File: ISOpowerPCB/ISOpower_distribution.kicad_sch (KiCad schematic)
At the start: 28 parts

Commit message: significant changes
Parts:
- added JP?: DSBL_BYPSS_A, symbol Jumper:SolderJumper_2_Open
- added JP?: DSBL_BYPSS_B, symbol Jumper:SolderJumper_2_Open
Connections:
- net GND: now also JP?.1 (A), JP?.1 (A)
- net at Q?.3 (S), U?.2 (On/Off): now also JP?.2 (B) (x2)
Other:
- moved on the sheet: C?
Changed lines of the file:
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@@
   (junction (at 41.91 143.51) (diameter 0) (color 0 0 0 0)
   )
+  (junction (at 50.8 166.37) (diameter 0) (color 0 0 0 0)
+  )
   (junction (at 57.15 87.63) (diameter 0) (color 0 0 0 0)
   )
@@
   (junction (at 207.01 74.93) (diameter 0) (color 0 0 0 0)
   )
+  (junction (at 59.69 153.67) (diameter 0) (color 0 0 0 0)
+  )
   (junction (at 107.95 64.77) (diameter 0) (color 0 0 0 0)
   )
@@
   (junction (at 158.75 130.81) (diameter 0) (color 0 0 0 0)
   )
-  (junction (at 40.64 64.77) (diameter 0) (color 0 0 0 0)
+  (junction (at 35.56 64.77) (diameter 0) (color 0 0 0 0)
   )
   (junction (at 90.17 87.63) (diameter 0) (color 0 0 0 0)
@@
   (junction (at 90.17 64.77) (diameter 0) (color 0 0 0 0)
   )
+  (junction (at 48.26 87.63) (diameter 0) (color 0 0 0 0)
+  )
   (junction (at 250.19 44.45) (diameter 0) (color 0 0 0 0)
   )
@@
   (junction (at 157.48 52.07) (diameter 0) (color 0 0 0 0)
   )
-  (junction (at 40.64 87.63) (diameter 0) (color 0 0 0 0)
+  (junction (at 35.56 87.63) (diameter 0) (color 0 0 0 0)
   )
   (junction (at 214.63 143.51) (diameter 0) (color 0 0 0 0)
+  )
+  (junction (at 57.15 74.93) (diameter 0) (color 0 0 0 0)
   )
   (junction (at 107.95 87.63) (diameter 0) (color 0 0 0 0)
@@
     (stroke (width 0) (type default) (color 0 0 0 0))
   )
-  (wire (pts (xy 39.37 80.01) (xy 41.91 80.01))
+  (wire (pts (xy 34.29 80.01) (xy 36.83 80.01))
     (stroke (width 0) (type default) (color 0 0 0 0))
   )
@@
     (stroke (width 0) (type default) (color 0 0 0 0))
   )
-  (wire (pts (xy 31.75 81.28) (xy 39.37 81.28))
+  (wire (pts (xy 26.67 81.28) (xy 34.29 81.28))
     (stroke (width 0) (type default) (color 0 0 0 0))
   )
@@
     (stroke (width 0) (type default) (color 0 0 0 0))
   )
+  (wire (pts (xy 50.8 166.37) (xy 59.69 166.37))
+    (stroke (width 0) (type default) (color 0 0 0 0))
+  )
   (wire (pts (xy 269.24 57.15) (xy 269.24 44.45))
     (stroke (width 0) (type default) (color 0 0 0 0))
@@
     (stroke (width 0) (type default) (color 0 0 0 0))
   )
+  (wire (pts (xy 57.15 74.93) (xy 48.26 74.93))
+    (stroke (width 0) (type default) (color 0 0 0 0))
+  )
   (wire (pts (xy 107.95 87.63) (xy 107.95 80.01))
     (stroke (width 0) (type default) (color 0 0 0 0))
@@
     (stroke (width 0) (type default) (color 0 0 0 0))
   )
+  (wire (pts (xy 50.8 163.83) (xy 50.8 166.37))
+    (stroke (width 0) (type default) (color 0 0 0 0))
+  )
   (wire (pts (xy 87.63 156.21) (xy 91.44 156.21))
     (stroke (width 0) (type default) (color 0 0 0 0))
@@
     (stroke (width 0) (type default) (color 0 0 0 0))
   )
-  (wire (pts (xy 39.37 81.28) (xy 39.37 80.01))
+  (wire (pts (xy 34.29 81.28) (xy 34.29 80.01))
     (stroke (width 0) (type default) (color 0 0 0 0))
   )
@@
     (stroke (width 0) (type default) (color 0 0 0 0))
   )
+  (wire (pts (xy 48.26 74.93) (xy 48.26 77.47))
+    (stroke (width 0) (type default) (color 0 0 0 0))
+  )
   (wire (pts (xy 59.69 166.37) (xy 63.5 166.37))
     (stroke (width 0) (type default) (color 0 0 0 0))
   )
-  (wire (pts (xy 40.64 77.47) (xy 40.64 87.63))
-    (stroke (width 0) (type default) (color 0 0 0 0))
-  )
-  (wire (pts (xy 41.91 166.37) (xy 59.69 166.37))
+  (wire (pts (xy 35.56 77.47) (xy 35.56 87.63))
+    (stroke (width 0) (type default) (color 0 0 0 0))
+  )
+  (wire (pts (xy 41.91 166.37) (xy 50.8 166.37))
     (stroke (width 0) (type default) (color 0 0 0 0))
   )
@@
     (stroke (width 0) (type default) (color 0 0 0 0))
   )
-  (wire (pts (xy 41.91 80.01) (xy 41.91 81.28))
+  (wire (pts (xy 36.83 80.01) (xy 36.83 81.28))
     (stroke (width 0) (type default) (color 0 0 0 0))
   )
@@
     (stroke (width 0) (type default) (color 0 0 0 0))
   )
-  (wire (pts (xy 40.64 64.77) (xy 62.23 64.77))
-    (stroke (width 0) (type default) (color 0 0 0 0))
-  )
   (wire (pts (xy 109.22 173.99) (xy 109.22 166.37))
     (stroke (width 0) (type default) (color 0 0 0 0))
@@
     (stroke (width 0) (type default) (color 0 0 0 0))
   )
+  (wire (pts (xy 35.56 64.77) (xy 62.23 64.77))
+    (stroke (width 0) (type default) (color 0 0 0 0))
+  )
   (wire (pts (xy 203.2 128.27) (xy 205.74 128.27))
     (stroke (width 0) (type default) (color 0 0 0 0))
@@
     (stroke (width 0) (type default) (color 0 0 0 0))
   )
-  (wire (pts (xy 40.64 87.63) (xy 57.15 87.63))
+  (wire (pts (xy 35.56 87.63) (xy 48.26 87.63))
     (stroke (width 0) (type default) (color 0 0 0 0))
   )
@@
     (stroke (width 0) (type default) (color 0 0 0 0))
   )
-  (wire (pts (xy 40.64 87.63) (xy 40.64 95.25))
+  (wire (pts (xy 35.56 87.63) (xy 35.56 95.25))
     (stroke (width 0) (type default) (color 0 0 0 0))
   )
@@
     (stroke (width 0) (type default) (color 0 0 0 0))
   )
+  (wire (pts (xy 48.26 85.09) (xy 48.26 87.63))
+    (stroke (width 0) (type default) (color 0 0 0 0))
+  )
   (wire (pts (xy 154.94 130.81) (xy 158.75 130.81))
     (stroke (width 0) (type default) (color 0 0 0 0))
@@
     (stroke (width 0) (type default) (color 0 0 0 0))
   )
+  (wire (pts (xy 48.26 87.63) (xy 57.15 87.63))
+    (stroke (width 0) (type default) (color 0 0 0 0))
+  )
   (wire (pts (xy 158.75 125.73) (xy 158.75 130.81))
     (stroke (width 0) (type default) (color 0 0 0 0))
@@
     (stroke (width 0) (type default) (color 0 0 0 0))
   )
-  (wire (pts (xy 35.56 64.77) (xy 40.64 64.77))
-    (stroke (width 0) (type default) (color 0 0 0 0))
-  )
   (wire (pts (xy 139.7 143.51) (xy 139.7 140.97))
     (stroke (width 0) (type default) (color 0 0 0 0))
@@
     (stroke (width 0) (type default) (color 0 0 0 0))
   )
-  (wire (pts (xy 40.64 64.77) (xy 40.64 69.85))
+  (wire (pts (xy 35.56 64.77) (xy 35.56 69.85))
     (stroke (width 0) (type default) (color 0 0 0 0))
   )
@@
     (stroke (width 0) (type default) (color 0 0 0 0))
   )
-  (wire (pts (xy 41.91 81.28) (xy 49.53 81.28))
+  (wire (pts (xy 50.8 153.67) (xy 59.69 153.67))
+    (stroke (width 0) (type default) (color 0 0 0 0))
+  )
+  (wire (pts (xy 36.83 81.28) (xy 49.53 81.28))
+    (stroke (width 0) (type default) (color 0 0 0 0))
+  )
+  (wire (pts (xy 50.8 156.21) (xy 50.8 153.67))
     (stroke (width 0) (type default) (color 0 0 0 0))
   )
@@
     (effects (font (size 1.27 1.27)) (justify right))
   )
-  (hierarchical_label "BUS_A_DISABLE" (shape input) (at 31.75 81.28 180)
+  (hierarchical_label "BUS_A_DISABLE" (shape input) (at 26.67 81.28 180)
     (effects (font (size 1.27 1.27)) (justify right))
   )
@@
     (pin "2")
   )
-  (symbol (lib_id "Device:100u") (at 40.64 73.66 0) (unit 1)
-    (in_bom yes) (on_board yes) (fields_autoplaced)
-    (property "Reference" "C?" (id 0) (at 44.45 71.5009 0)
-      (effects (font (size 1.27 1.27)) (justify left))
-    )
-    (property "Value" "100u" (id 1) (at 44.45 74.0409 0)
-      (effects (font (size 1.27 1.27)) (justify left))
-    )
-    (property "Footprint" "Capacitor_SMD:CP_Elec_10x10" (id 2) (at 41.6052 77.47 0)
-      (effects (font (size 1.27 1.27)) hide)
-    )
-    (property "Datasheet" "~" (id 3) (at 40.64 73.66 0)
+  (symbol (lib_id "Device:100u") (at 35.56 73.66 0) (unit 1)
+    (in_bom yes) (on_board yes) (fields_autoplaced)
+    (property "Reference" "C?" (id 0) (at 39.37 71.5009 0)
+      (effects (font (size 1.27 1.27)) (justify left))
+    )
+    (property "Value" "100u" (id 1) (at 39.37 74.0409 0)
+      (effects (font (size 1.27 1.27)) (justify left))
+    )
+    (property "Footprint" "Capacitor_SMD:CP_Elec_10x10" (id 2) (at 36.5252 77.47 0)
+      (effects (font (size 1.27 1.27)) hide)
+    )
+    (property "Datasheet" "~" (id 3) (at 35.56 73.66 0)
       (effects (font (size 1.27 1.27)) hide)
     )
@@
     (pin "14")
     (pin "7")
+  )
+  (symbol (lib_id "Jumper:SolderJumper_2_Open") (at 48.26 81.28 90) (unit 1)
+    (in_bom yes) (on_board yes)
+    (property "Reference" "JP?" (id 0) (at 45.72 86.36 90))
+    (property "Value" "DSBL_BYPSS_A" (id 1) (at 46.99 90.17 90))
+    (property "Footprint" "" (id 2) (at 48.26 81.28 0)
+      (effects (font (size 1.27 1.27)) hide)
+    )
+    (property "Datasheet" "~" (id 3) (at 48.26 81.28 0)
+      (effects (font (size 1.27 1.27)) hide)
+    )
+    (pin "1")
+    (pin "2")
   )
   (symbol (lib_id "power:GND") (at 109.22 173.99 0) (unit 1)
@@
     (pin "1")
   )
-  (symbol (lib_id "power:GND") (at 40.64 95.25 0) (unit 1)
-    (in_bom yes) (on_board yes) (fields_autoplaced)
-    (property "Reference" "#PWR?" (id 0) (at 40.64 101.6 0)
-      (effects (font (size 1.27 1.27)) hide)
-    )
-    (property "Value" "GND" (id 1) (at 40.64 100.33 0))
-    (property "Footprint" "" (id 2) (at 40.64 95.25 0)
-      (effects (font (size 1.27 1.27)) hide)
-    )
-    (property "Datasheet" "" (id 3) (at 40.64 95.25 0)
-      (effects (font (size 1.27 1.27)) hide)
-    )
+  (symbol (lib_id "Jumper:SolderJumper_2_Open") (at 50.8 160.02 90) (unit 1)
+    (in_bom yes) (on_board yes)
+    (property "Reference" "JP?" (id 0) (at 48.26 165.1 90))
+    (property "Value" "DSBL_BYPSS_B" (id 1) (at 49.53 168.91 90))
+    (property "Footprint" "" (id 2) (at 50.8 160.02 0)
+      (effects (font (size 1.27 1.27)) hide)
+    )
+    (property "Datasheet" "~" (id 3) (at 50.8 160.02 0)
+      (effects (font (size 1.27 1.27)) hide)
+    )
+    (pin "1")
+    (pin "2")
+  )
+  (symbol (lib_id "power:GND") (at 35.56 95.25 0) (unit 1)
+    (in_bom yes) (on_board yes) (fields_autoplaced)
+    (property "Reference" "#PWR?" (id 0) (at 35.56 101.6 0)
+      (effects (font (size 1.27 1.27)) hide)
+    )
+    (property "Value" "GND" (id 1) (at 35.56 100.33 0))
+    (property "Footprint" "" (id 2) (at 35.56 95.25 0)
+      (effects (font (size 1.27 1.27)) hide)
+    )
+    (property "Datasheet" "" (id 3) (at 35.56 95.25 0)
+      (effects (font (size 1.27 1.27)) hide)
+    )

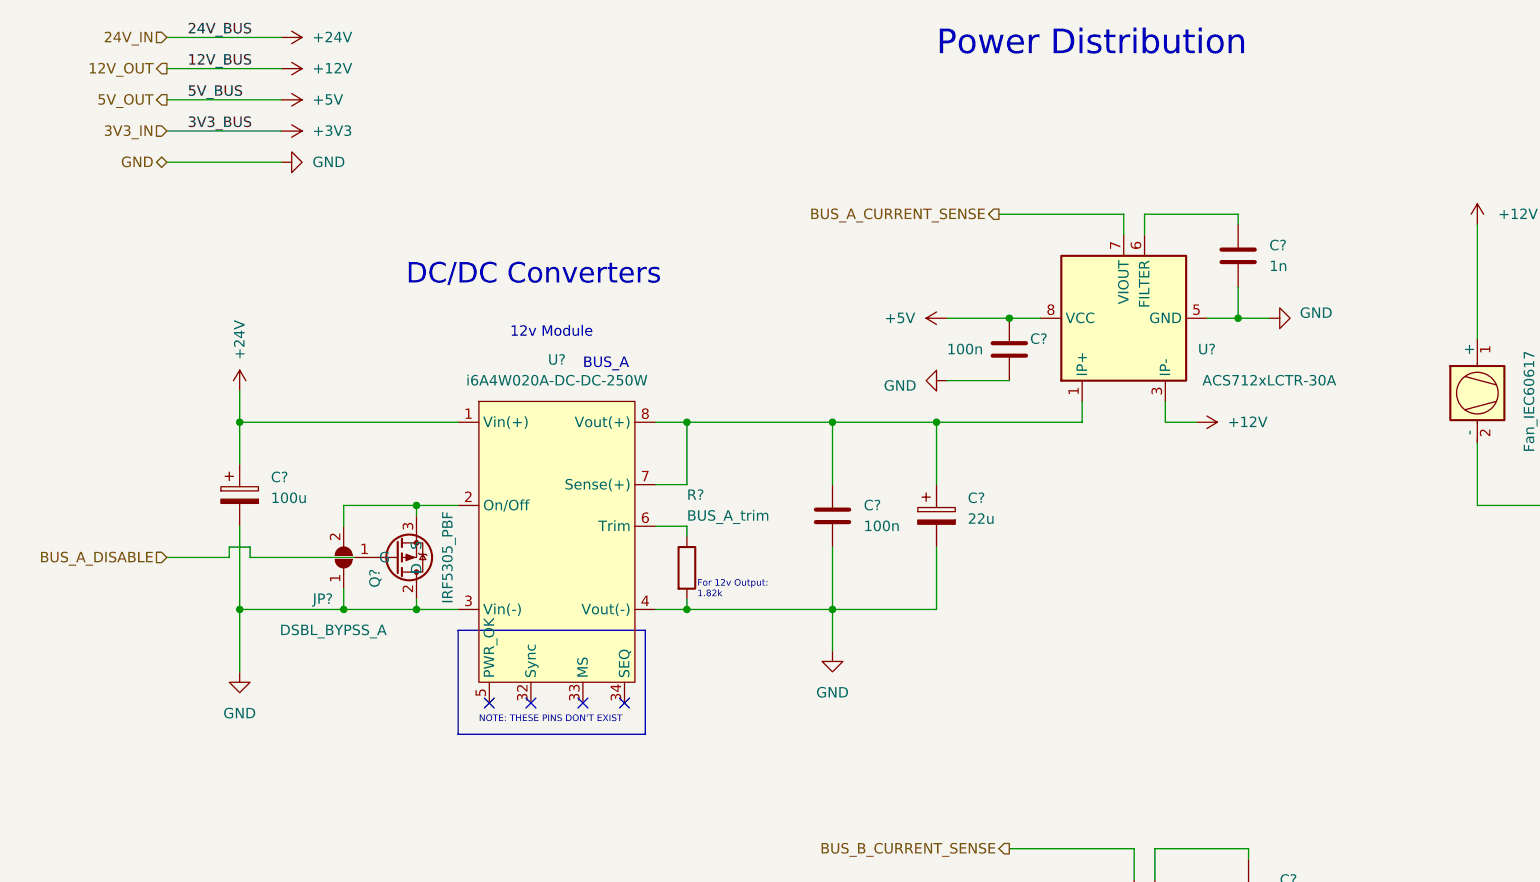
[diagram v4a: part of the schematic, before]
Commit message: Updated as per discussions 26/01/22
# Change Notes

04/02/2022
As per discussion 26/01/22
1. Changed per channel 5v MOSFET switches to MOSFET control of DC/DC module on/off pin - due to failure of MOSFET switching during testing.
2. Added 5v buck converter for independent MCU_5V power bus.
	- Ensured all 5v MCU hardware is powered from common MCU_5V bus.
3. Removed circuit from NC pins on DC/DC modules.
4. Changed ESP32 USB interface to CH340
5. Changed MCU serial logic level converters from MOSFET to IC - TXS0102DCT
	- TODO: OE pin now requires low signal untill DC/DC supply is stable - Does it? Can it just be tied to 5v bus with a large capacitor? Does it need MCU to hold pin low untill 5V_BUS is stable?
6. Removed redundent 3V3_IN to power distribution page.
	- Rechecked all sheets for redundent pins, it won't impact drawing traces, but it will impact readability.
7. Added Mechanical layer as hirarchical sheet.
8. Moved voltage monitoring circuits to hirarchical sheet
9. Added voltage monitoring with TL431DBZ to 12V_BUS
10. Automatic shutoff circuit removed, as this would prevent the DC/DC module from powering on. Instead moved to AtMega328p digital inputs
and microcontroller will control shutdown of DC/DC supply if out of spec voltage detected.
		- This is a severe limitation compared to the specification, and this also does not prevent damage to devices on 5V_BUS if voltage is pulled high, for example to 12v due to user error.
		- TODO: Add independent overvoltage protection to 5V_BUS? 		[Zener Diode Overvoltage Protection - Sparkfun](https://www.rs-online.com/designspark/how-does-zener-diode-do-overvoltage-protection-in-circuit#:~:text=In%20order%20to%20protect%20the,flow%20in%20the%20reverse%20direction).
11. Changed logic level conversion for 12v outputs to 12v drive circuit. [12v drive circuit](https://forum.arduino.cc/t/easiest-way-of-driving-amplifying-from-5v-to-12v/123290)
12. Added proto pin connections for ESP MCU.
13. Changed 20v Zener in reverse vol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
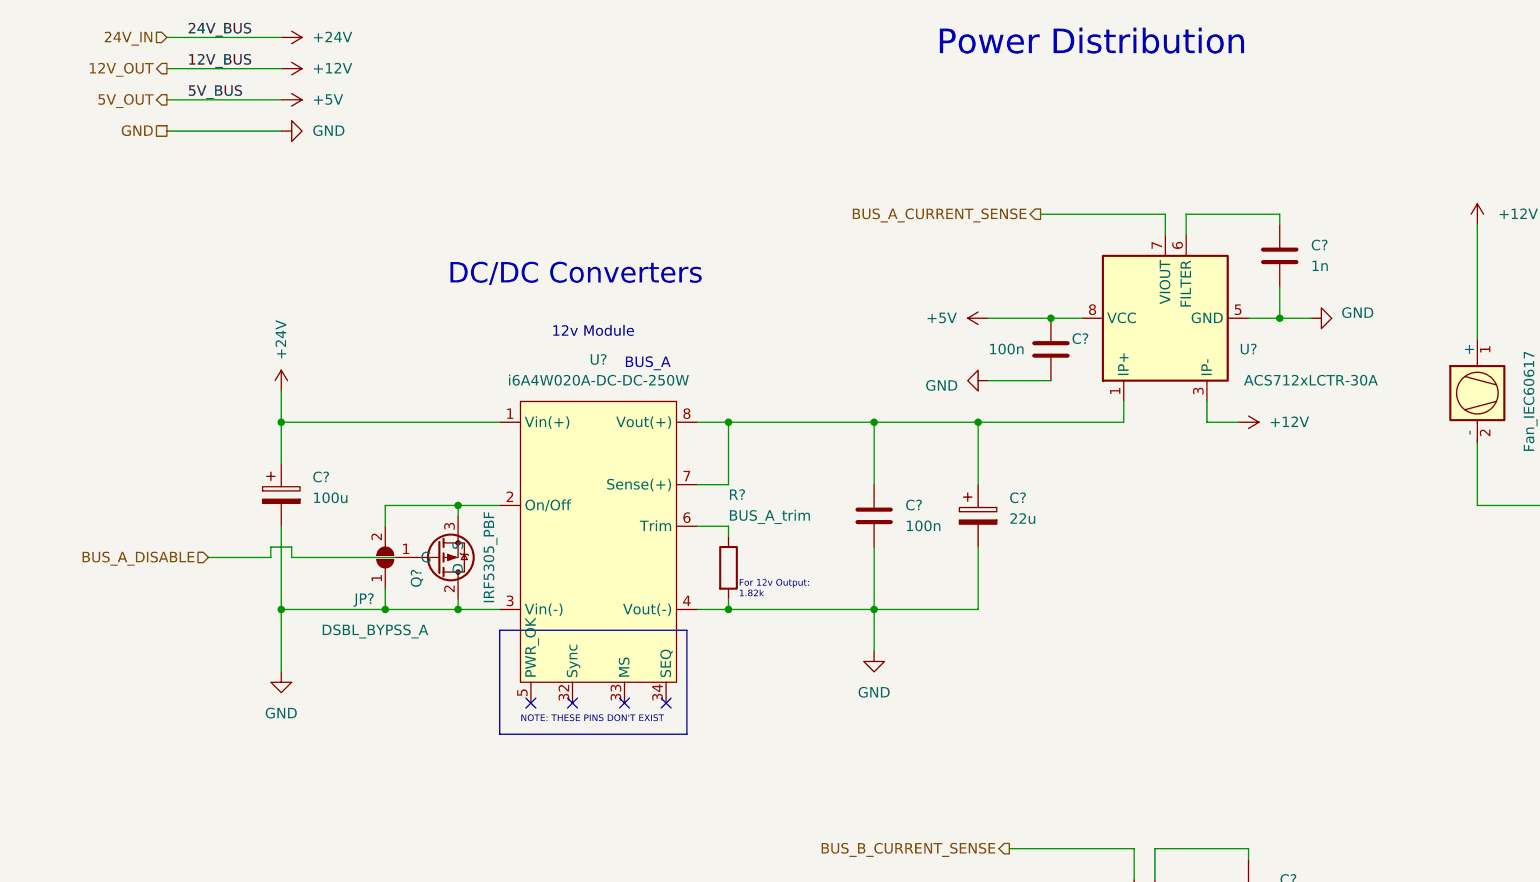
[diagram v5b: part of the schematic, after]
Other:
- moved on the sheet: C?, JP?, Q?, R?, U?

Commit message: messing around with libraries
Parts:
- C11, C12, C15, C16, C17, C18: renamed from C?; symbol 000_Capacitor_film_immo:cap_film_0805 -> 000_Capacitor_FIlm_Immo:cap_film_0805
- gave numbers to parts that had none: 24

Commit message: adding logic for fault indication
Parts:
- C10, C21, C9: symbol Device:100u -> 000_Capacitor_Electrolytic_Immo:100u
- C13, C14: symbol 000_Capacitor_electrolytic_immo:22u -> 000_Capacitor_Electrolytic_Immo:22u
- C19: symbol 000_Capacitor_electrolytic_immo:100u -> 000_Capacitor_Electrolytic_Immo:680u
- C20: symbol 000_Capacitor_electrolytic_immo:100u -> 000_Capacitor_Electrolytic_Immo:220u
- M1: symbol 000_protection_immo:Fan_IEC60617 -> 009_Heat_Management_Immo:Fan_IEC60617
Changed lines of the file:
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@@
     (pin "2")
   )
-  (symbol (lib_id "000_Capacitor_electrolytic_immo:100u") (at 259.08 138.43 0) (unit 1)
+  (symbol (lib_id "000_Capacitor_Electrolytic_Immo:220u") (at 259.08 138.43 0) (unit 1)
     (in_bom yes) (on_board yes)
     (property "Reference" "C20" (id 0) (at 262.89 136.2709 0)
@@
     (pin "1")
   )
-  (symbol (lib_id "000_Capacitor_electrolytic_immo:100u") (at 205.74 135.89 0) (unit 1)
+  (symbol (lib_id "000_Capacitor_Electrolytic_Immo:680u") (at 205.74 135.89 0) (unit 1)
     (in_bom yes) (on_board yes)
     (property "Reference" "C19" (id 0) (at 209.55 133.7309 0)
@@
     (pin "1")
   )
-  (symbol (lib_id "000_Capacitor_electrolytic_immo:22u") (at 121.92 154.94 0) (unit 1)
+  (symbol (lib_id "000_Capacitor_Electrolytic_Immo:22u") (at 121.92 154.94 0) (unit 1)
     (in_bom yes) (on_board yes) (fields_autoplaced)
     (property "Reference" "C13" (id 0) (at 125.73 152.7809 0)
@@
     (pin "2")
   )
-  (symbol (lib_id "000_protection_immo:Fan_IEC60617") (at 186.69 62.23 0) (unit 1)
+  (symbol (lib_id "009_Heat_Management_Immo:Fan_IEC60617") (at 186.69 62.23 0) (unit 1)
     (in_bom yes) (on_board yes)
     (property "Reference" "M1" (id 0) (at 195.58 62.23 90))
@@
     (pin "1")
   )
-  (symbol (lib_id "Device:100u") (at 269.24 60.96 0) (unit 1)
+  (symbol (lib_id "000_Capacitor_Electrolytic_Immo:100u") (at 269.24 60.96 0) (unit 1)
     (in_bom yes) (on_board yes) (fields_autoplaced)
     (property "Reference" "C21" (id 0) (at 273.05 58.8009 0)
@@
     (pin "2")
   )
-  (symbol (lib_id "Device:100u") (at 40.64 73.66 0) (unit 1)
+  (symbol (lib_id "000_Capacitor_Electrolytic_Immo:100u") (at 40.64 73.66 0) (unit 1)
     (in_bom yes) (on_board yes) (fields_autoplaced)
     (property "Reference" "C9" (id 0) (at 44.45 71.5009 0)
@@
     (pin "2")
   )
-  (symbol (lib_id "000_Capacitor_electrolytic_immo:22u") (at 125.73 76.2 0) (unit 1)
+  (symbol (lib_id "000_Capacitor_Electrolytic_Immo:22u") (at 125.73 76.2 0) (unit 1)
     (in_bom yes) (on_board yes) (fields_autoplaced)
     (property "Reference" "C14" (id 0) (at 129.54 74.0409 0)
@@
     (pin "1")
   )
-  (symbol (lib_id "Device:100u") (at 41.91 149.86 0) (unit 1)
+  (symbol (lib_id "000_Capacitor_Electrolytic_Immo:100u") (at 41.91 149.86 0) (unit 1)
     (in_bom yes) (on_board yes) (fields_autoplaced)
     (property "Reference" "C10" (id 0) (at 45.72 147.7009 0)
